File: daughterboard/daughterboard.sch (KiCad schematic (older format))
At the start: 19 parts, among them J1 Conn_02x07_Odd_Even, J2 Conn_01x01, J3 Conn_01x01, J4 Conn_01x01, J5 Conn_01x01, SW1 SW_Push, SW2 Rotary_Encoder_Switch_Alps, SW3 SW_Push, SW4 SW_Push

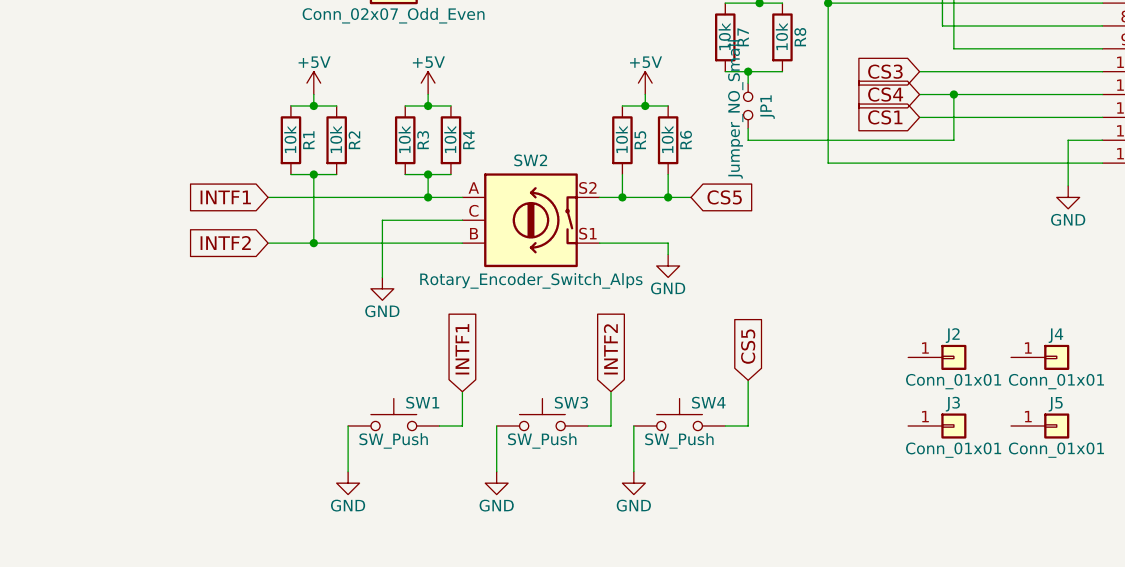
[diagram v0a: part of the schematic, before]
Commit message: Added debouncing capacitors
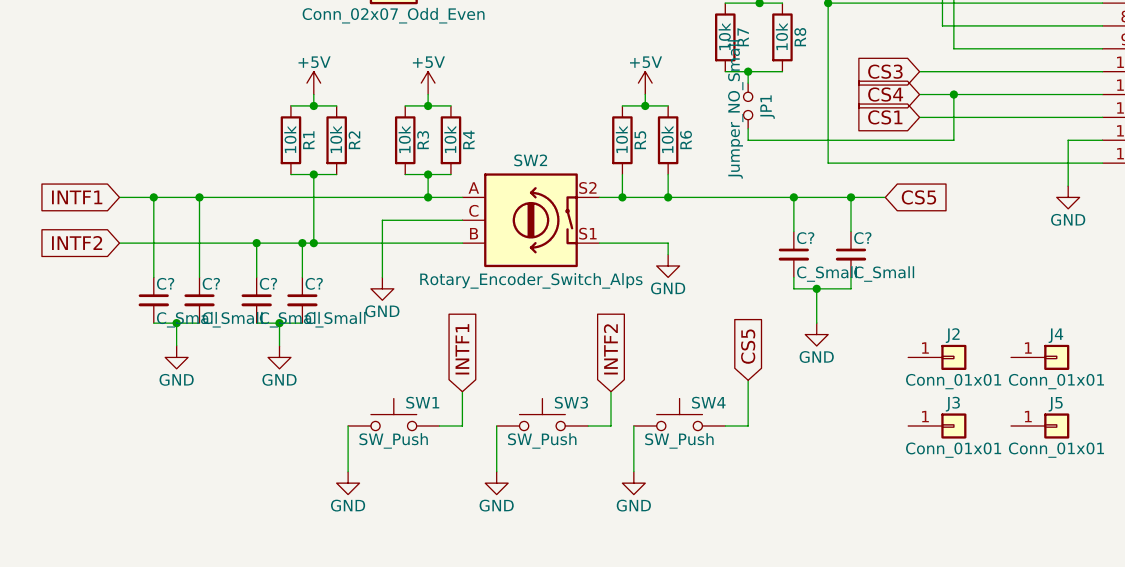
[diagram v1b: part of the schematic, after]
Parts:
- added C? (x3): C_Small, Capacitors_SMD:C_0805_HandSoldering, symbol C_Small
- added C? (x3): C_Small, Capacitors_THT:C_Disc_D5.0mm_W2.5mm_P2.50mm, symbol C_Small
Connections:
- net CS5: now also C?.1, C?.1
- net GND: now also C?.2, C?.2, C?.2, C?.2, C?.2, C?.2
- net INTF1: now also C?.1, C?.1
- net INTF2: now also C?.1, C?.1
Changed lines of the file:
@@
 	1    0    0    -1
 $EndComp
-Text GLabel 3650 4150 2    60   Input ~ 0
+Text GLabel 4500 4150 2    60   Input ~ 0
 CS5
 $Comp
@@
 	5300 3900 5450 3900
 Wire Wire Line
-	3250 4150 3650 4150
+	3250 4150 4500 4150
 Wire Wire Line
 	3550 4400 3550 4350
@@
 	2400 4050 2600 4050
 Wire Wire Line
-	1800 4150 2650 4150
+	1150 4150 2650 4150
 Wire Wire Line
 	2500 4150 2500 4050
@@
 	1900 4050 2100 4050
 Wire Wire Line
-	2000 4050 2000 4350
-Wire Wire Line
-	1800 4350 2650 4350
+	2000 4350 2000 4050
+Wire Wire Line
+	1150 4350 2650 4350
 Connection ~ 2000 4050
-Text GLabel 1800 4150 0    60   Input ~ 0
+Text GLabel 1150 4150 0    60   Input ~ 0
 INTF1
 Connection ~ 2500 4150
@@
 Wire Wire Line
 	3900 5150 3800 5150
-Text GLabel 1800 4350 0    60   Input ~ 0
+Text GLabel 1150 4350 0    60   Input ~ 0
 INTF2
 Text GLabel 2650 5000 1    60   Input ~ 0
@@
 	1    0    0    -1
 $EndComp
+$Comp
+L C_Small C?
+U 1 1 5DB04AB0
+P 1300 4600
+F 0 "C?" H 1310 4670 50  0000 L CNN
+F 1 "C_Small" H 1310 4520 50  0000 L CNN
+F 2 "Capacitors_SMD:C_0805_HandSoldering" H 1300 4600 50  0001 C CNN
+F 3 "" H 1300 4600 50  0001 C CNN
+	1    1300 4600
+	1    0    0    -1
+$EndComp
+$Comp
+L C_Small C?
+U 1 1 5DB04B22
+P 1500 4600
+F 0 "C?" H 1510 4670 50  0000 L CNN
+F 1 "C_Small" H 1510 4520 50  0000 L CNN
+F 2 "Capacitors_THT:C_Disc_D5.0mm_W2.5mm_P2.50mm" H 1500 4600 50  0001 C CNN
+F 3 "" H 1500 4600 50  0001 C CNN
+	1    1500 4600
+	1    0    0    -1
+$EndComp
+Wire Wire Line
+	1500 4500 1500 4150
+Connection ~ 1500 4150
+Wire Wire Line
+	1300 4500 1300 4150
+Connection ~ 1300 4150
+Wire Wire Line
+	1300 4700 1500 4700
+$Comp
+L GND #PWR?
+U 1 1 5DB04E59
+P 1400 4800
+F 0 "#PWR?" H 1400 4550 50  0001 C CNN
+F 1 "GND" H 1400 4650 50  0000 C CNN
+F 2 "" H 1400 4800 50  0001 C CNN
+F 3 "" H 1400 4800 50  0001 C CNN
+	1    1400 4800
+	1    0    0    -1
+$EndComp
+Wire Wire Line
+	1400 4800 1400 4700
+Connection ~ 1400 4700
+$Comp
+L C_Small C?
+U 1 1 5DB04F23
+P 1750 4600
+F 0 "C?" H 1760 4670 50  0000 L CNN
+F 1 "C_Small" H 1760 4520 50  0000 L CNN
+F 2 "Capacitors_SMD:C_0805_HandSoldering" H 1750 4600 50  0001 C CNN
+F 3 "" H 1750 4600 50  0001 C CNN
+	1    1750 4600
+	1    0    0    -1
+$EndComp
+$Comp
+L C_Small C?
+U 1 1 5DB04F79
+P 1950 4600
+F 0 "C?" H 1960 4670 50  0000 L CNN
+F 1 "C_Small" H 1960 4520 50  0000 L CNN
+F 2 "Capacitors_THT:C_Disc_D5.0mm_W2.5mm_P2.50mm" H 1950 4600 50  0001 C CNN
+F 3 "" H 1950 4600 50  0001 C CNN
+	1    1950 4600
+	1    0    0    -1
+$EndComp
+Wire Wire Line
+	1750 4700 1950 4700
+$Comp
+L GND #PWR?
+U 1 1 5DB05040
+P 1850 4800
+F 0 "#PWR?" H 1850 4550 50  0001 C CNN
+F 1 "GND" H 1850 4650 50  0000 C CNN
+F 2 "" H 1850 4800 50  0001 C CNN
+F 3 "" H 1850 4800 50  0001 C CNN
+	1    1850 4800
+	1    0    0    -1
+$EndComp
+Wire Wire Line
+	1850 4800 1850 4700
+Connection ~ 1850 4700
+Wire Wire Line
+	1950 4500 1950 4350
+Connection ~ 1950 4350
+Wire Wire Line
+	1750 4500 1750 4350
+Connection ~ 1750 4350
+$Comp
+L C_Small C?
+U 1 1 5DB0532D
+P 4100 4400
+F 0 "C?" H 4110 4470 50  0000 L CNN
+F 1 "C_Small" H 4110 4320 50  0000 L CNN
+F 2 "Capacitors_SMD:C_0805_HandSoldering" H 4100 4400 50  0001 C CNN
+F 3 "" H 4100 4400 50  0001 C CNN
+	1    4100 4400
+	1    0    0    -1
+$EndComp
+$Comp
+L C_Small C?
+U 1 1 5DB0539D
+P 4350 4400
+F 0 "C?" H 4360 4470 50  0000 L CNN
+F 1 "C_Small" H 4360 4320 50  0000 L CNN
+F 2 "Capacitors_THT:C_Disc_D5.0mm_W2.5mm_P2.50mm" H 4350 4400 50  0001 C CNN
+F 3 "" H 4350 4400 50  0001 C CNN
+	1    4350 4400
+	1    0    0    -1
+$EndComp
+Wire Wire Line
+	4100 4300 4100 4150
+Connection ~ 4100 4150
+Wire Wire Line
+	4350 4300 4350 4150
+Connection ~ 4350 4150
+Wire Wire Line
+	4100 4500 4100 4550
+Wire Wire Line
+	4100 4550 4350 4550
+Wire Wire Line
+	4350 4550 4350 4500
+$Comp
+L GND #PWR?
+U 1 1 5DB055E7
+P 4200 4700
+F 0 "#PWR?" H 4200 4450 50  0001 C CNN
+F 1 "GND" H 4200 4550 50  0000 C CNN
+F 2 "" H 4200 4700 50  0001 C CNN
+F 3 "" H 4200 4700 50  0001 C CNN
+	1    4200 4700
+	1    0    0    -1
+$EndComp
+Wire Wire Line
+	4200 4700 4200 4550
+Connection ~ 4200 4550
 $EndSCHEMATC

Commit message: Added resistors in discharge debounce
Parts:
- added R10, R12, R14: 100R, Resistors_THT:R_Axial_DIN0207_L6.3mm_D2.5mm_P7.62mm_Horizontal, symbol R
- added R11, R13, R9: 100R, Resistors_SMD:R_0805_HandSoldering, symbol R
- C1, C2, C3, C4, C5, C6: renamed from C?; value C_Small -> 100 nF
- R1, R2, R3, R4, R5, R6, R7, R8: value 10k -> 100k
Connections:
- net CS5: now also R13.1, R14.1; no longer C5.1, C6.1
- net INTF1: now also R10.1, R9.1; no longer C1.1, C2.1
- net INTF2: now also R11.1, R12.1; no longer C3.1, C4.1
- new net: C1.1, C2.1, R10.2, R9.2
- new net: C3.1, C4.1, R11.2, R12.2
- new net: C5.1, C6.1, R13.2, R14.2
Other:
- moved on the sheet: C1, C2, C3, C4, C5, C6

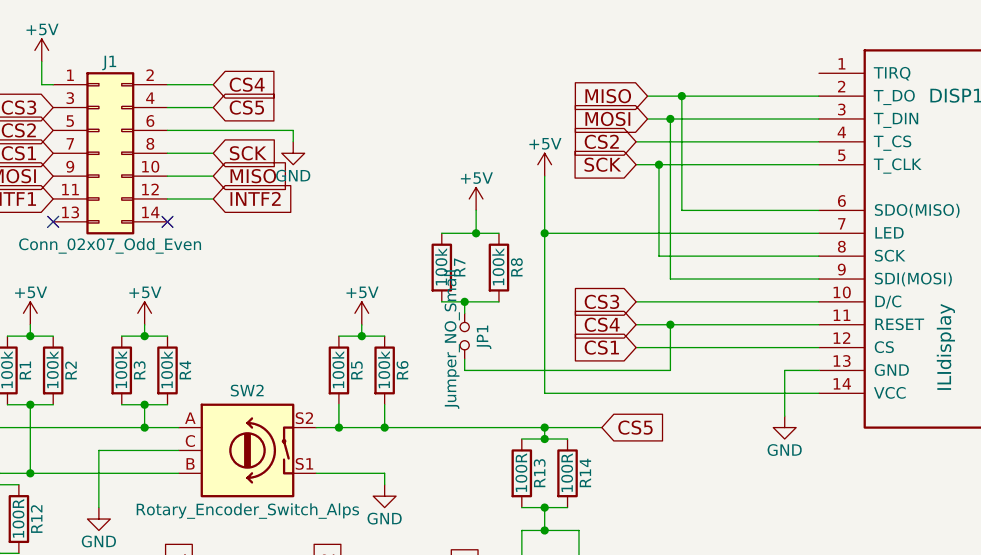
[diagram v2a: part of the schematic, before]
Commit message: Added vacuum holes to fixture
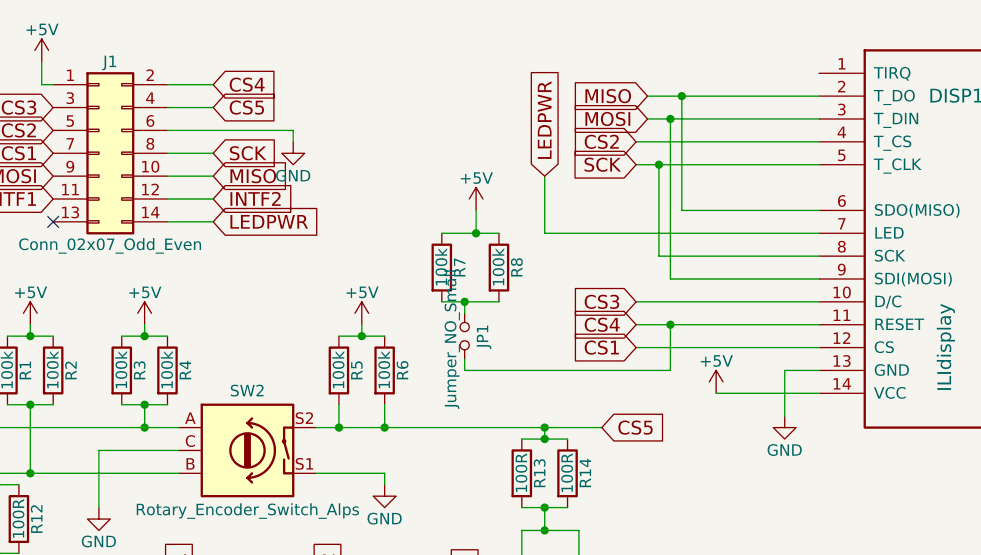
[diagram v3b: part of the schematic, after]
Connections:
- net +5V: no longer DISP1.7 (LED)
- net LEDPWR: now reaches J1.14 (Pin_14)
- net LEDPWR: now also DISP1.7 (LED)
- no-connect marks 2 -> 1
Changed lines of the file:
@@
 L +5V #PWR14
 U 1 1 5DAF73DB
-P 4250 3050
-F 0 "#PWR14" H 4250 2900 50  0001 C CNN
-F 1 "+5V" H 4250 3190 50  0000 C CNN
-F 2 "" H 4250 3050 50  0001 C CNN
-F 3 "" H 4250 3050 50  0001 C CNN
-	1    4250 3050
+P 5000 4000
+F 0 "#PWR14" H 5000 3850 50  0001 C CNN
+F 1 "+5V" H 5000 4140 50  0000 C CNN
+F 2 "" H 5000 4000 50  0001 C CNN
+F 3 "" H 5000 4000 50  0001 C CNN
+	1    5000 4000
 	1    0    0    -1
 $EndComp
@@
 	4650 3600 5450 3600
 Wire Wire Line
-	4250 3050 4250 4000
+	4250 3050 4250 3300
 Wire Wire Line
 	4250 3300 5450 3300
-Wire Wire Line
-	4250 4000 5450 4000
-Connection ~ 4250 3300
 Wire Wire Line
 	5300 4100 5300 3900
@@
 by Daniel Marks KW4TI
 NoConn ~ 2100 3250
-NoConn ~ 2600 3250
 Wire Wire Line
 	3900 3900 3900 3850
@@
 Connection ~ 1850 4400
 Connection ~ 1850 4350
+Text GLabel 2800 3250 2    60   Input ~ 0
+LEDPWR
+Wire Wire Line
+	2600 3250 2800 3250
+Text GLabel 4250 3050 1    60   Input ~ 0
+LEDPWR
+Wire Wire Line
+	5000 4000 5450 4000
 $EndSCHEMATC

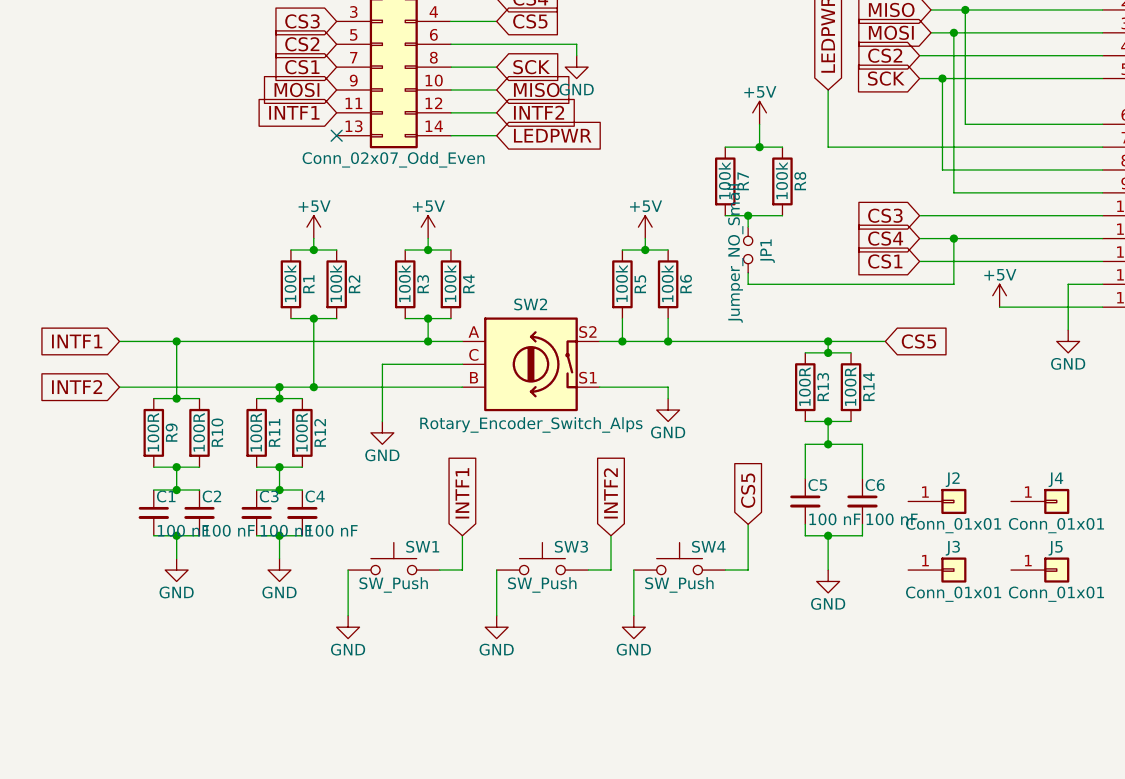
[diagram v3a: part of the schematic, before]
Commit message: Added jogwheel and sweep, simplified daughterboard
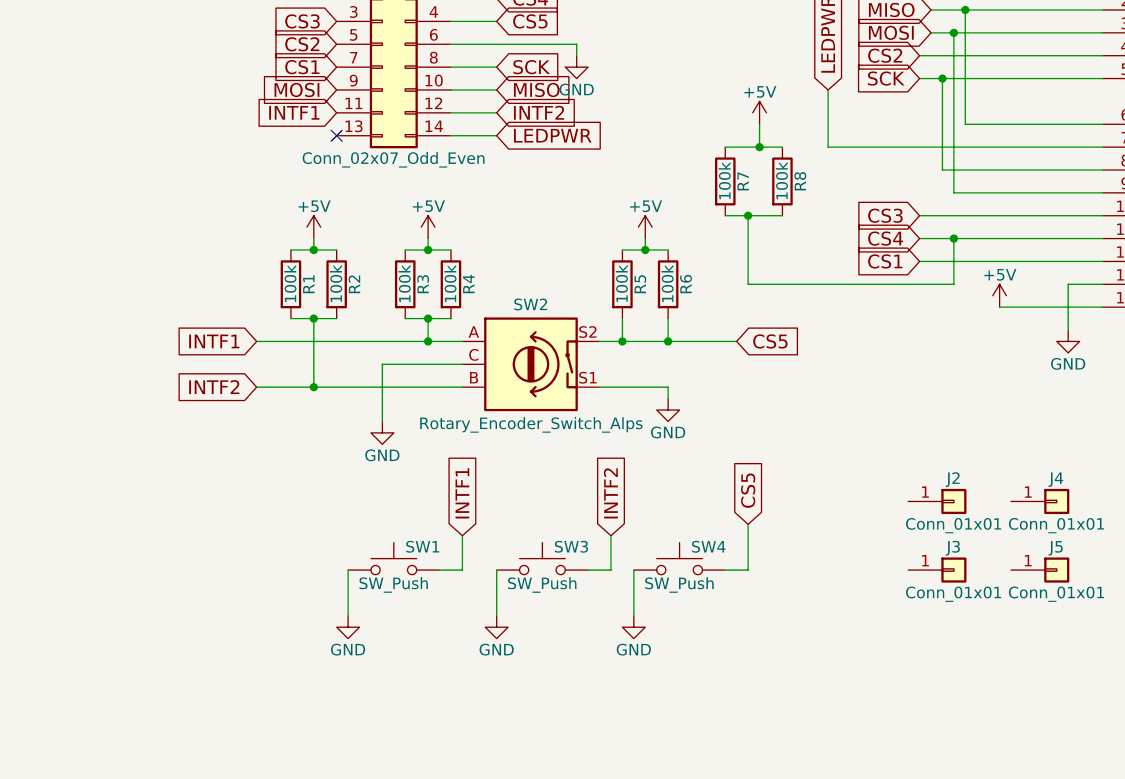
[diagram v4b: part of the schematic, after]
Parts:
- removed C1, C3, C5: 100 nF, Capacitors_SMD:C_0805_HandSoldering, symbol C_Small
- removed C2, C4, C6: 100 nF, Capacitors_THT:C_Disc_D5.0mm_W2.5mm_P2.50mm, symbol C_Small
- removed JP1: Jumper_NO_Small, Pin_Headers:Pin_Header_Straight_1x02_Pitch2.54mm, symbol Jumper_NO_Small
- removed R10, R12, R14: 100R, Resistors_THT:R_Axial_DIN0207_L6.3mm_D2.5mm_P7.62mm_Horizontal, symbol R
- removed R11, R13, R9: 100R, Resistors_SMD:R_0805_HandSoldering, symbol R
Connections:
- net CS4: now also R7.2, R8.2
